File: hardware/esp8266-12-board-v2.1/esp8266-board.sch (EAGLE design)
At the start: 26 parts, among them J1 DEBUG, J2 WATCHDOG, P3 GND DTR RTS RX TX

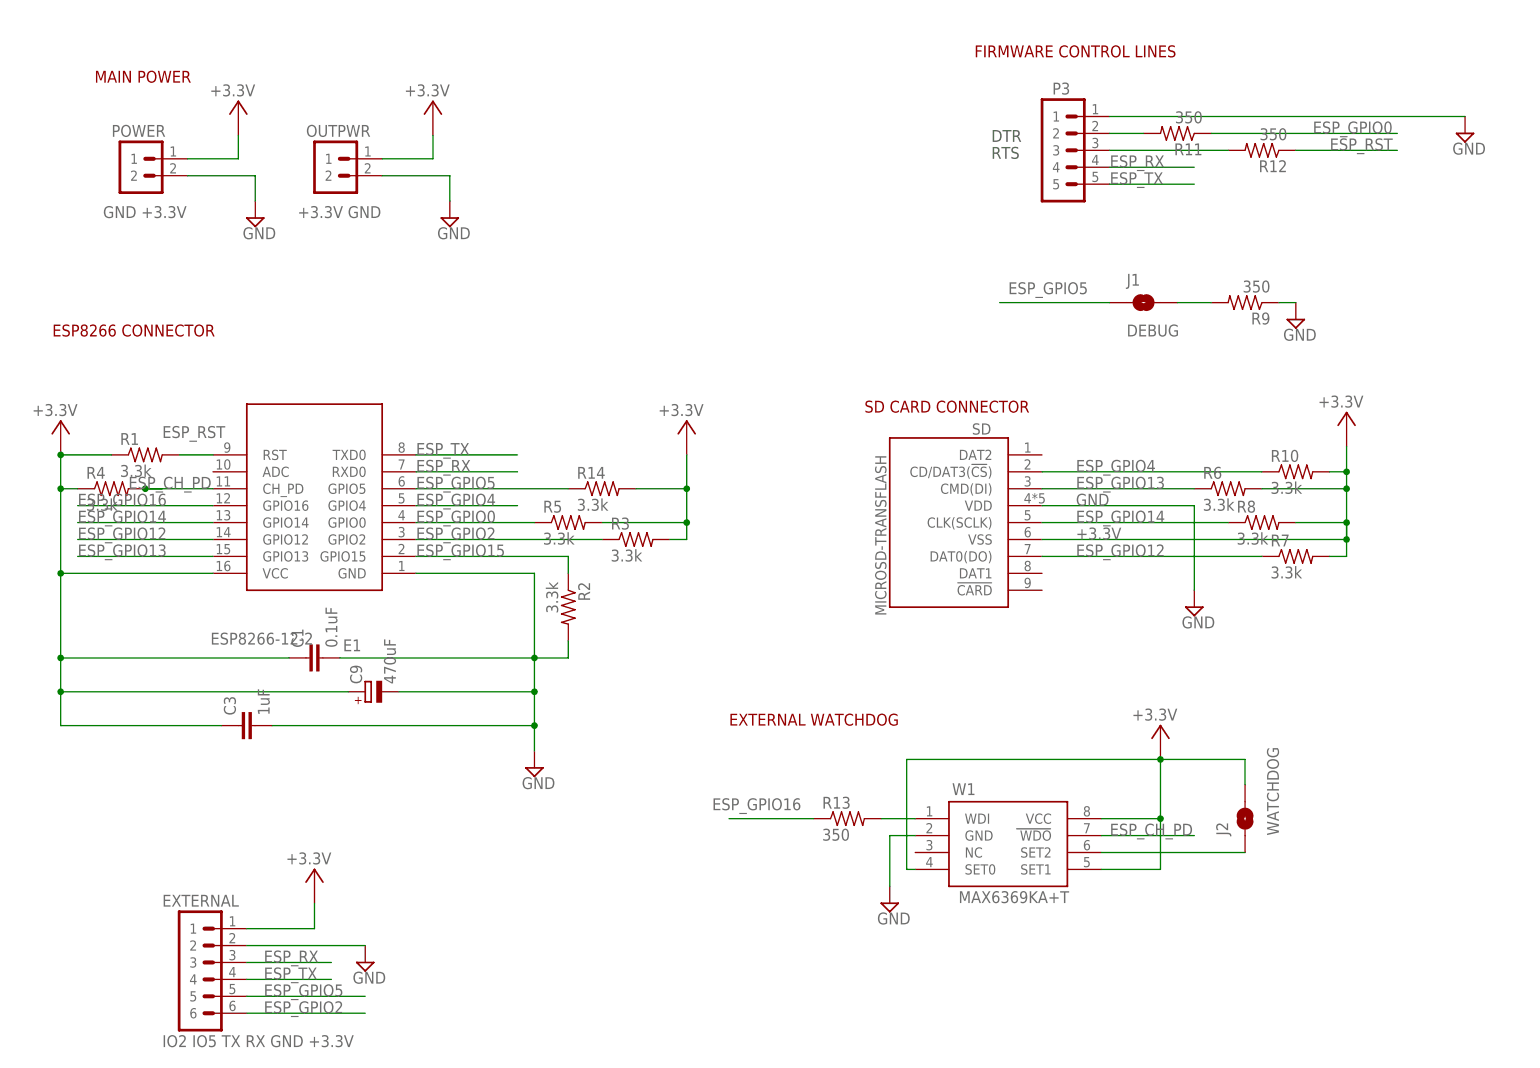
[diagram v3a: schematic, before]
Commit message: PCB revision to v2.1
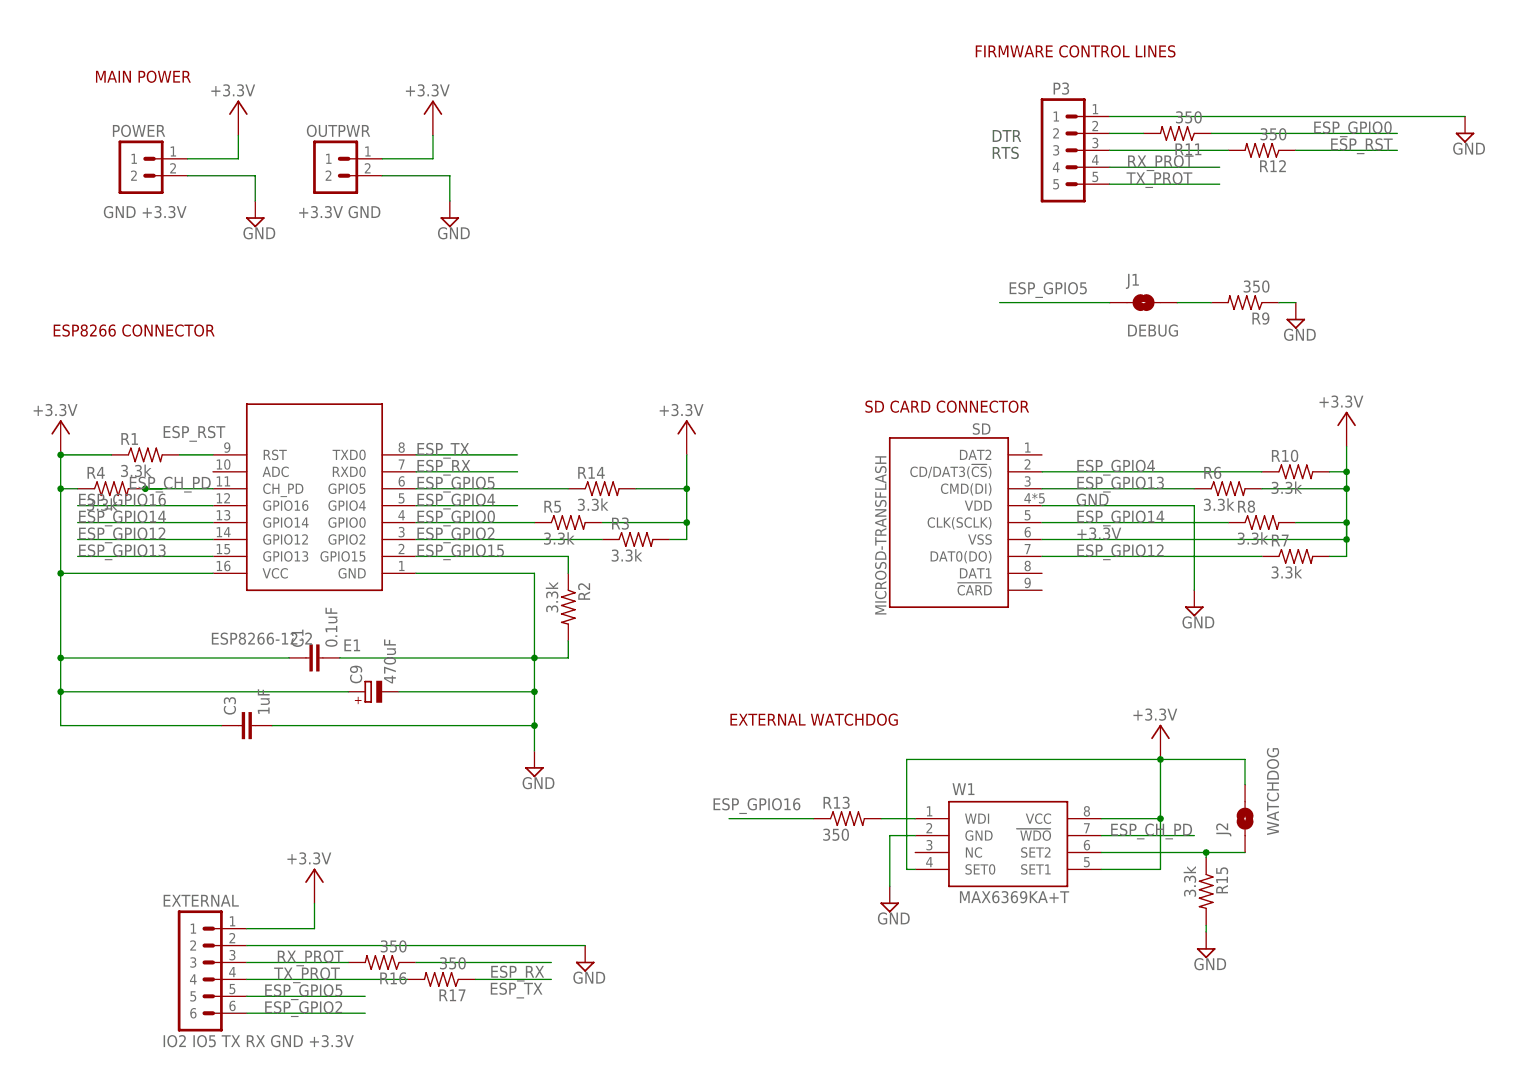
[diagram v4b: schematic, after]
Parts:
- added R15: 3.3k, stutz-components-library:RESISTOR0805
- added R16, R17: 350, stutz-components-library:RESISTOR0805
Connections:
- new net RX_PROT: EXTERNAL.3, P3.4, R16.2
- new net TX_PROT: EXTERNAL.4, P3.5, R17.2
- net ESP_RX: now also R16.1; no longer EXTERNAL.3, P3.4
- net ESP_TX: now also R17.1; no longer EXTERNAL.4, P3.5
- net GND: now also R15.2
- net N$1: now also R15.1
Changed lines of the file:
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@@
 <setting verticaltext="up"/>
 </settings>
-<grid distance="0.1" unitdist="inch" unit="inch" style="lines" multiple="1" display="no" altdistance="0.01" altunitdist="inch" altunit="inch"/>
+<grid distance="0.05" unitdist="inch" unit="inch" style="lines" multiple="1" display="yes" altdistance="0.01" altunitdist="inch" altunit="inch"/>
 <layers>
 <layer number="1" name="Top" color="4" fill="1" visible="no" active="no"/>
@@
 <part name="SUPPLY1" library="supply2" deviceset="GND" device=""/>
 <part name="SUPPLY3" library="stutz-eagle" deviceset="+3.3V" device=""/>
+<part name="R15" library="stutz-components-library" deviceset="RESISTOR" device="0805" value="3.3k"/>
+<part name="SUPPLY11" library="supply2" deviceset="GND" device=""/>
+<part name="R16" library="stutz-components-library" deviceset="RESISTOR" device="0805" value="350"/>
+<part name="R17" library="stutz-components-library" deviceset="RESISTOR" device="0805" value="350"/>
 </parts>
 <sheets>
@@
 <instance part="R8" gate="G$1" x="193.04" y="93.98"/>
 <instance part="R10" gate="G$1" x="198.12" y="101.6"/>
-<instance part="SUPPLY18" gate="GND" x="58.42" y="27.94"/>
+<instance part="SUPPLY18" gate="GND" x="91.44" y="27.94"/>
 <instance part="SUPPLY10" gate="G$1" x="39.37" y="154.67"/>
 <instance part="SUPPLY8" gate="G$1" x="50.8" y="39.37"/>
@@
 <instance part="SUPPLY1" gate="GND" x="71.12" y="139.7"/>
 <instance part="SUPPLY3" gate="G$1" x="68.58" y="154.67"/>
+<instance part="R15" gate="G$1" x="184.658" y="38.608" rot="R270"/>
+<instance part="SUPPLY11" gate="GND" x="184.658" y="29.972"/>
+<instance part="R16" gate="G$1" x="60.96" y="27.94" rot="R180"/>
+<instance part="R17" gate="G$1" x="69.85" y="25.4" rot="R180"/>
 </instances>
 <busses>
@@
 <pinref part="EXTERNAL" gate="G$1" pin="2"/>
 <pinref part="SUPPLY18" gate="GND" pin="GND"/>
-<wire x1="40.64" y1="30.48" x2="58.42" y2="30.48" width="0.1524" layer="91"/>
+<wire x1="40.64" y1="30.48" x2="91.44" y2="30.48" width="0.1524" layer="91"/>
 </segment>
 <segment>
@@
 <pinref part="OUTPWR" gate="G$1" pin="2"/>
 <wire x1="60.96" y1="146.05" x2="71.12" y2="146.05" width="0.1524" layer="91"/>
+</segment>
+<segment>
+<pinref part="SUPPLY11" gate="GND" pin="GND"/>
+<pinref part="R15" gate="G$1" pin="2"/>
+<wire x1="184.658" y1="32.512" x2="184.658" y2="33.528" width="0.1524" layer="91"/>
 </segment>
 </net>
@@
 </segment>
 <segment>
-<pinref part="P3" gate="G$1" pin="5"/>
-<wire x1="170.18" y1="144.78" x2="182.88" y2="144.78" width="0.1524" layer="91"/>
-<label x="170.18" y="144.78" size="1.778" layer="95"/>
-</segment>
-<segment>
-<wire x1="40.64" y1="25.4" x2="53.34" y2="25.4" width="0.1524" layer="91"/>
-<label x="43.18" y="25.4" size="1.778" layer="95"/>
-<pinref part="EXTERNAL" gate="G$1" pin="4"/>
+<wire x1="74.93" y1="25.4" x2="86.36" y2="25.4" width="0.1524" layer="91"/>
+<pinref part="R17" gate="G$1" pin="1"/>
+<label x="85.09" y="24.892" size="1.778" layer="95" rot="R180"/>
 </segment>
 </net>
@@
 </segment>
 <segment>
-<pinref part="P3" gate="G$1" pin="4"/>
-<wire x1="170.18" y1="147.32" x2="182.88" y2="147.32" width="0.1524" layer="91"/>
-<label x="170.18" y="147.32" size="1.778" layer="95"/>
-</segment>
-<segment>
-<wire x1="40.64" y1="27.94" x2="53.34" y2="27.94" width="0.1524" layer="91"/>
-<label x="43.18" y="27.94" size="1.778" layer="95"/>
-<pinref part="EXTERNAL" gate="G$1" pin="3"/>
+<wire x1="66.04" y1="27.94" x2="86.36" y2="27.94" width="0.1524" layer="91"/>
+<pinref part="R16" gate="G$1" pin="1"/>
+<label x="85.344" y="27.432" size="1.778" layer="95" rot="R180"/>
 </segment>
 </net>
@@
 <pinref part="W1" gate="G$1" pin="SET2"/>
 <pinref part="J2" gate="G$1" pin="1"/>
-<wire x1="168.91" y1="44.45" x2="190.5" y2="44.45" width="0.1524" layer="91"/>
+<wire x1="168.91" y1="44.45" x2="184.658" y2="44.45" width="0.1524" layer="91"/>
+<pinref part="R15" gate="G$1" pin="1"/>
+<wire x1="184.658" y1="44.45" x2="190.5" y2="44.45" width="0.1524" layer="91"/>
+<wire x1="184.658" y1="43.688" x2="184.658" y2="44.45" width="0.1524" layer="91"/>
+<junction x="184.658" y="44.45"/>
 </segment>
 </net>
@@
 </segment>
 </net>
+<net name="RX_PROT" class="0">
+<segment>
+<pinref part="EXTERNAL" gate="G$1" pin="3"/>
+<wire x1="40.64" y1="27.94" x2="55.88" y2="27.94" width="0.1524" layer="91"/>
+<pinref part="R16" gate="G$1" pin="2"/>
+<label x="55.118" y="29.718" size="1.778" layer="95" rot="R180"/>
+</segment>
+<segment>
+<pinref part="P3" gate="G$1" pin="4"/>
+<wire x1="170.18" y1="147.32" x2="186.69" y2="147.32" width="0.1524" layer="91"/>
+<label x="172.72" y="147.32" size="1.778" layer="95"/>
+</segment>
+</net>
+<net name="TX_PROT" class="0">
+<segment>
+<pinref part="EXTERNAL" gate="G$1" pin="4"/>
+<wire x1="40.64" y1="25.4" x2="64.77" y2="25.4" width="0.1524" layer="91"/>
+<pinref part="R17" gate="G$1" pin="2"/>
+<label x="54.61" y="27.178" size="1.778" layer="95" rot="R180"/>
+</segment>
+<segment>
+<pinref part="P3" gate="G$1" pin="5"/>
+<wire x1="170.18" y1="144.78" x2="186.69" y2="144.78" width="0.1524" layer="91"/>
+<label x="172.72" y="144.78" size="1.778" layer="95"/>
+</segment>
+</net>

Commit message: updated pcb after first manufacturing impressions
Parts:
- C1: value 0.1uF -> 100nF
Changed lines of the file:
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@@
 <setting verticaltext="up"/>
 </settings>
-<grid distance="0.05" unitdist="inch" unit="inch" style="lines" multiple="1" display="yes" altdistance="0.01" altunitdist="inch" altunit="inch"/>
+<grid distance="0.1" unitdist="inch" unit="inch" style="lines" multiple="1" display="no" altdistance="0.01" altunitdist="inch" altunit="inch"/>
 <layers>
 <layer number="1" name="Top" color="4" fill="1" visible="no" active="no"/>
@@
 <part name="P3" library="stutz-components-library" deviceset="PIN-HEADER-5PIN" device="" value="GND DTR RTS  RX   TX"/>
 <part name="SUPPLY7" library="supply2" deviceset="GND" device=""/>
-<part name="C1" library="stutz-components-library" deviceset="CAPACITOR" device="0805" value="0.1uF"/>
+<part name="C1" library="stutz-components-library" deviceset="CAPACITOR" device="0805" value="100nF"/>
 <part name="E1" library="stutz-components-library" deviceset="ESP8266-12-2" device=""/>
 <part name="SUPPLY13" library="supply2" deviceset="GND" device=""/>
